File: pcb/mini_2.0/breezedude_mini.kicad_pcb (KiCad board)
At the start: 2 copper layers, 53 x 22.2 mm, 43 parts, among them J1 USB_C_Receptacle_USB2.0_16P, J2 Conn_01x02_Socket, J3 Conn_01x04_Pin, J4 Conn_01x02_Pin, J5 Conn_01x04_Pin, J6 Conn_01x04_Pin, J7 Conn_01x02_Pin, Q1 PMOS, SW1 SW_Push, U1 ATSAMD21G18A-A, U2 RFM95W-868S2, U3 BMP280, U4 AP2112K-3.3, U5 PMIC-CN3063_SOIC8_, U6 BMP388

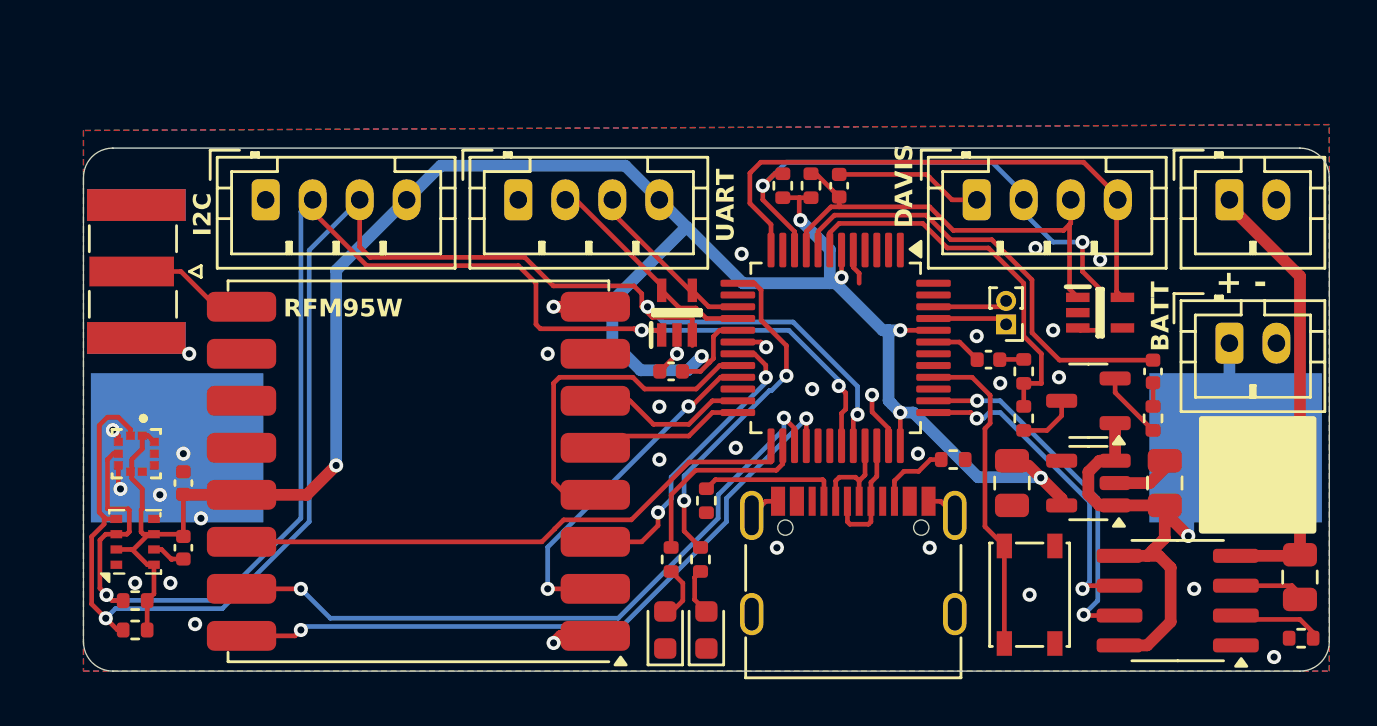
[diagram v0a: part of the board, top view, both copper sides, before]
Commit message: v2.1. fixed p-fet, added vollgo cc68, vertical SMA
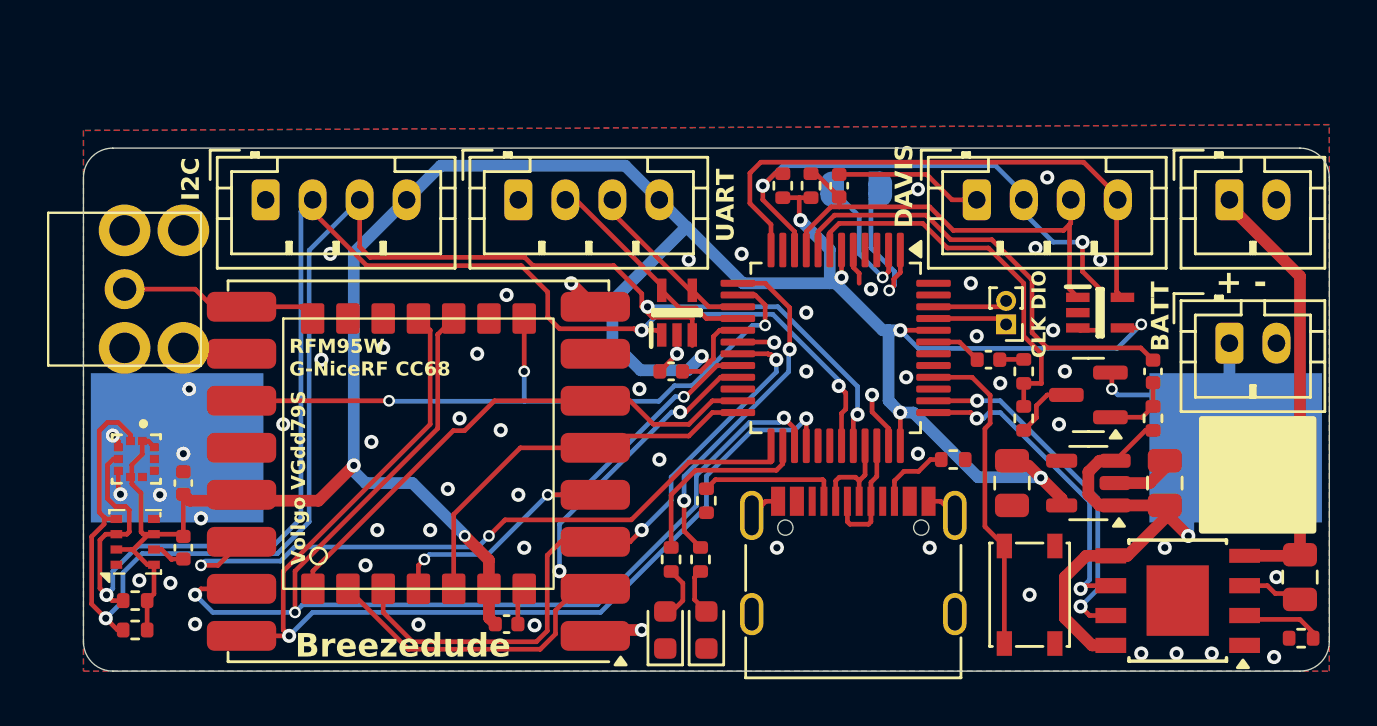
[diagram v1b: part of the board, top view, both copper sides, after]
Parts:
- removed Q1: PMOS, Package_TO_SOT_SMD:SOT-23-3
- added C10: 10u 6.3V, Capacitor_SMD:C_0402_1005Metric, F.Cu at (115.0, 122.0)
- added J8: Conn_01x02_Pin, general:SolderJumper-2_Open_Gap1mm, B.Cu at (130.2, 103.5)
- added Q2: IRLML6401, Package_TO_SOT_SMD:SOT-23, F.Cu at (139.8, 112.2)
- added U8: ~, LoRa:vollgo_vgdd79s868n0s1, F.Cu at (111.2, 114.8)
- AE1: footprint Connector_Coaxial:SMA_Samtec_SMA-J-P-X-ST-EM1_EdgeMount -> LoRa:sma_edge_6.5mm_vert
- U5: footprint Package_SO:SOIC-8_3.9x4.9mm_P1.27mm -> Package_SO:Infineon_PG-DSO-8-43
- moved AE1 0.90 mm to (98.8, 107.8), turned to 90 degrees
- moved U6 0.23 mm to (99.2, 115.0)
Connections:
- net /EN_HEATER renamed /EN_DCDC
- net /RFM_CS renamed /LORA_CS
- net /RFM_DIO0 renamed /LORA_DIO0
- net /RFM_DIO1 renamed /LORA_DIO1
- net /RFM_DIO2 renamed /LORA_DIO2
- net /RFM_MISO renamed /LORA_MISO
- net /RFM_MOSI renamed /LORA_MOSI
- net /RFM_RESET renamed /LORA_RESET
- net /RFM_SCK renamed /LORA_SCK
- net /SPI_MISO renamed /D36
- D2 pad 4: unconnected-(D2-I/O4-Pad4) -> /3V3
- R7 pad 1: Net-(Q1-G) -> /BATT+
- U1 pad 14: /D3 -> /LORA_DIO3
- U2 pad 11: unconnected-(U2-DIO3-Pad11) -> /LORA_DIO3
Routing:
- net /LORA_DIO3: track 0.00 -> 29.3 mm, vias 0 -> 3
- net /3V3: track 96.5 -> 118.9 mm, vias 7 -> 9
- net /LORA_DIO1: track 29.1 -> 48.9 mm, vias 2 -> 3
- net /LORA_DIO2: track 29.4 -> 45.9 mm
- net /LORA_RESET: track 6.64 -> 22.6 mm
- net /LORA_MOSI: track 12.8 -> 27.5 mm
- net /LORA_MISO: track 15.1 -> 27.5 mm
- net /LORA_CS: track 6.43 -> 16.8 mm
- net /BATT+: track 27.7 -> 35.5 mm, vias 1 -> 2
- net /TX1: track 0.00 -> 6.89 mm, vias 0 -> 1
- net /RX1: track 0.00 -> 5.91 mm, vias 0 -> 1
- net /LORA_SCK: track 15.0 -> 20.5 mm, vias 0 -> 3
- net /LORA_DIO0: track 24.4 -> 28.9 mm, vias 0 -> 2
- net Net-(Q1-G): track 2.88 -> 0.00 mm
- net Net-(Q2-G): track 1.01 -> 3.27 mm
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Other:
- board text added: "RFM95W G-NiceRF CC68"
- board text added: "RX1 TX1"
- board text added: "V2.1"
- board text added: "Vollgo VGdd79S"
- board text removed: "RFM95W"
- board text removed: "V2.0"

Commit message: mini V2.2
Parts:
- removed the BT1 at (120.5, 85.5)
- removed C7: 10u 6.3V, Capacitor_SMD:C_0402_1005Metric
- removed the J2 at (136.2, 109.2)
- removed the R8 at (126.8, 103.3)
- removed the U2 at (111.2, 115.5)
- removed the U3 at (99.2, 118.5)
- removed the U6 at (99.2, 115.0)
- added C11: 100n 16V, Capacitor_SMD:C_0402_1005Metric, F.Cu at (134.9, 111.3)
- added C12: 47u 6.3V, Capacitor_SMD:C_0805_2012Metric, F.Cu at (112.4, 121.2)
- added D5: Diode, Diode_SMD:D_SOD-123, F.Cu at (147.0, 116.6)
- added J4: Conn_01x03_Pin, Connector_PinHeader_1.00mm:PinHeader_1x03_P1.00mm_Vertical, F.Cu at (135.1, 107.5)
- added JP1: SolderJumper_2_Open, Jumper:SolderJumper-2_P1.3mm_Open_RoundedPad1.0x1.5mm, F.Cu at (145.9, 114.3)
- added Q1: P-MOS, Package_TO_SOT_SMD:SOT-23, F.Cu at (138.6, 108.6)
- added U4: LIS2MDL, Package_LGA:LGA-12_2x2mm_P0.5mm, F.Cu at (79.0, 121.0)
- added U5: BMP280, Package_LGA:Bosch_LGA-8_2x2.5mm_P0.65mm_ClockwisePinNumbering, F.Cu at (75.3, 117.2)
- added U7: BMP388, footprints_flo:PQFN50P200X200X80-10N, F.Cu at (75.2, 120.7)
- added U8: HP203B, Sensors:HP203B-LGA8, F.Cu at (99.5, 115.5)
- C10: value 10u 6.3V -> 220n 16V
- Q2: value IRLML6401 -> P-MOS
- R2: renamed from R9; value 10k -> 100k
- R6: renamed from R10; value 100 -> 470
- U2: renamed from U4; value AP2112K-3.3 -> STLQ015M33R
- moved C10 36.7 mm to (78.8, 116.1), turned to 0 degrees
- moved C8 6.08 mm to (99.6, 112.9), turned to 180 degrees
- moved R8 4.21 mm to (98.5, 118.1)
- moved R9 3.31 mm to (100.8, 118.1)
- moved U6 2.98 mm to (108.5, 113.6)
- moved R5 2.60 mm to (135.4, 113.3), turned to -90 degrees
- moved J2 2.51 mm to (107.2, 103.7)
- moved J5 2.02 mm to (117.5, 103.7)
- moved D1 1.74 mm to (142.0, 108.7), turned to -90 degrees
- moved C6 1.23 mm to (123.2, 111.5), turned to 90 degrees
- moved R2 0.95 mm to (128.9, 103.3), turned to -90 degrees
- moved C5 0.90 mm to (130.0, 103.3)
- moved R11 0.78 mm to (133.2, 115.1)
- moved C2 0.72 mm to (136.0, 111.3), turned to 90 degrees
- moved C9 0.69 mm to (141.8, 111.3)
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- renumbered BT3 to BT1, C9 to C1, C1 to C2, C2 to C9, D2 to D1, D4 to D2, D1 to D3, D3 to D4, J7 to J1, J6 to J2, J5 to J3, J3 to J5, J4 to J6, J1 to J7, R11 to R1, R2 to R10, R1 to R11, R7 to R3, R5 to R4, R6 to R5, R12 to R7, R3 to R8, R4 to R9, U5 to U1, U1 to U3, U8 to U6
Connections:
- C10 pad 1: GND -> Net-(U4-C1)
- C10 pad 2: /3V3 -> GND
- C4 pad 2: /3V3 -> 3V3
- C6 pad 2: /3V3 -> 3V3
- C8 pad 2: /3V3 -> 3V3
- D1 pad 4: /3V3 -> 3V3
- J2 pad 4: /3V3 -> 3V3
- J5 pad 4: /3V3 -> VCC_WS
- R2 pad 1: /3V3 -> 3V3
- R8 pad 2: /3V3 -> 3V3
- R9 pad 2: /3V3 -> 3V3
- U2 pad 5: /3V3 -> 3V3
- U3 pad 17: /3V3 -> 3V3
- U3 pad 36: /3V3 -> 3V3
- U3 pad 44: /3V3 -> 3V3
- U3 pad 48: /D36 -> SW_WS
- U3 pad 6: /3V3 -> 3V3
- U6 pad 6: /3V3 -> 3V3
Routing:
- net /3V3: track 118.9 -> 0.00 mm, vias 9 -> 0
- net 3V3: track 0.00 -> 102.6 mm, vias 0 -> 10
- net /LORA_DIO0: track 28.9 -> 0.00 mm, vias 2 -> 0
- net Net-(JP1-A): track 0.00 -> 28.4 mm, vias 0 -> 2
- net /LORA_DIO1: track 48.9 -> 22.5 mm, vias 3 -> 2
- net /LORA_DIO2: track 45.9 -> 23.5 mm
- net VCC_WS: track 0.00 -> 19.1 mm, vias 0 -> 1
- net /SCL: track 69.5 -> 55.2 mm
- net /LORA_DIO3: track 29.3 -> 15.4 mm, vias 3 -> 2
- net /SDA: track 63.5 -> 52.9 mm
- net GND: track 31.2 -> 23.1 mm, vias 59 -> 53
- net SW_WS: track 0.00 -> 5.19 mm
- net /DAVIS_DIR: track 25.2 -> 20.3 mm
- net /LORA_MISO: track 27.5 -> 23.1 mm, vias 2 -> 0
- net /ANT: track 9.02 -> 5.29 mm
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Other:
- board size 53 x 22.2 mm -> 53 x 22.5 mm
- board text added: "BATT+"
- board text added: "C D G"
- board text added: "CLK DIO GND"
- board text added: "J1"
- board text added: "V2.2"
- board text removed: "CLK DIO"
- board text removed: "RFM95W G-NiceRF CC68"
- board text removed: "V2.1"
